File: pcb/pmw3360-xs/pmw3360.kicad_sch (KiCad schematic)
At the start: 16 parts, among them IC1001 AP7335-WG-7, J1001 Conn_01x01_Socket, J1002 Conn_01x01_Socket, J1004 Conn_01x01_Socket, J1005 Conn_01x01_Socket, J1006 Conn_01x01_Socket, J1007 Conn_01x01_Socket, U1001 PMW3360DM-T2QU

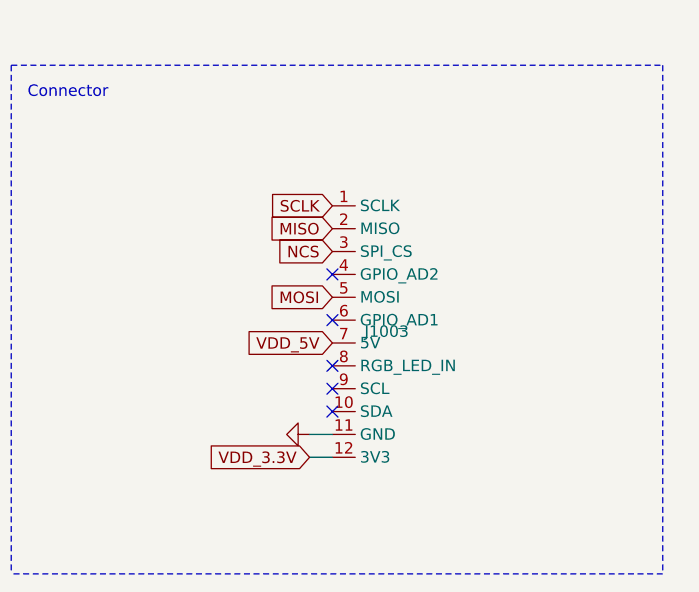
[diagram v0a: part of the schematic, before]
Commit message: updated vikm connector symbols, per some recommendations from sigprof in fingerpunch discord
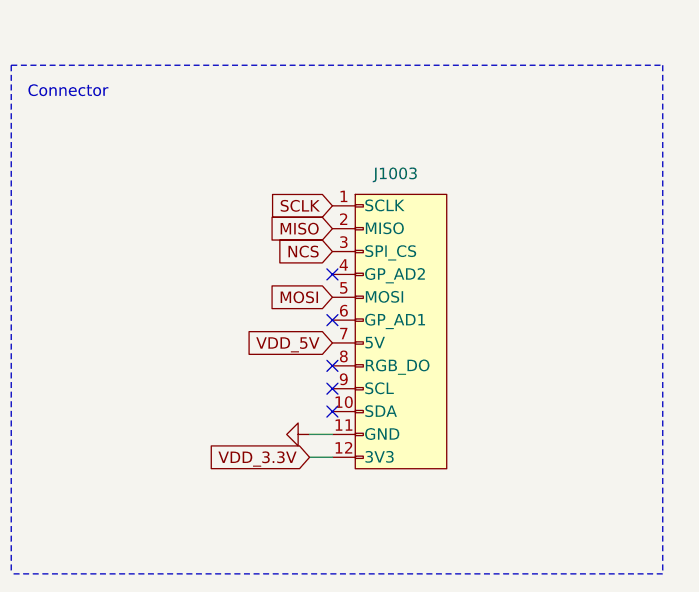
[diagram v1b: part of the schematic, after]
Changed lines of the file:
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@@
     )
   )
-  (symbol (lib_id "vik:vik-module-connector") (at 186.182 132.334 0) (unit 1)
-    (in_bom yes) (on_board yes) (dnp no) (fields_autoplaced)
-    (property "Reference" "J1003" (at 189.738 132.334 0)
+  (symbol (lib_id "vik:vik-module-connector") (at 193.802 131.064 0) (unit 1)
+    (in_bom yes) (on_board yes) (dnp no)
+    (property "Reference" "J1003" (at 190.754 114.808 0)
       (effects (font (size 1.27 1.27)) (justify left))
     )
-    (property "Value" "~" (at 186.182 125.984 0)
+    (property "Value" "~" (at 193.802 124.714 0)
       (effects (font (size 1.27 1.27)))
     )
-    (property "Footprint" "vik:vik-module-connector-horizontal" (at 186.182 125.984 0)
+    (property "Footprint" "vik:vik-module-connector-horizontal" (at 193.802 124.714 0)
       (effects (font (size 1.27 1.27)) hide)
     )
-    (property "Datasheet" "" (at 186.182 125.984 0)
+    (property "Datasheet" "" (at 193.802 124.714 0)
       (effects (font (size 1.27 1.27)) hide)
     )
-    (property "LCSC" "C2919557" (at 186.182 132.334 0)
+    (property "LCSC" "C2919557" (at 193.802 131.064 0)
       (effects (font (size 1.27 1.27)) hide)
     )

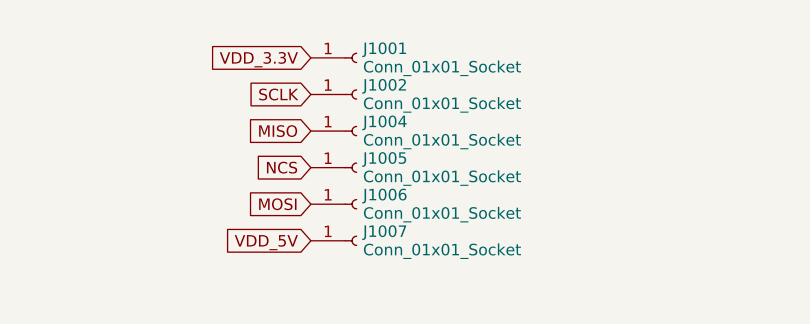
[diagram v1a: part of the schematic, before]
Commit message: added ground through hole for vik pmw3360 xs
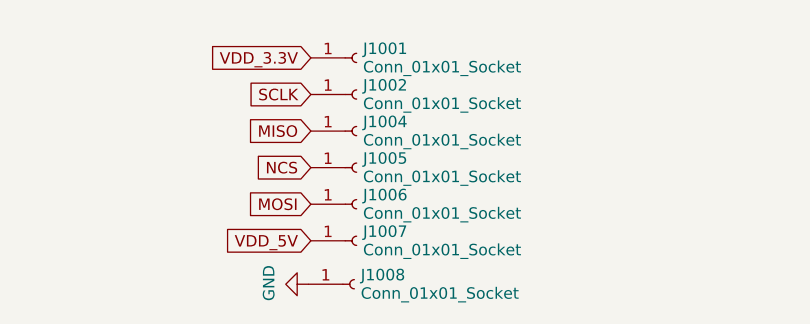
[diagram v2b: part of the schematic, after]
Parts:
- added J1008: Conn_01x01_Socket, Connector_Wire:SolderWire-0.5sqmm_1x01_D0.9mm_OD2.3mm, symbol Connector:Conn_01x01_Socket
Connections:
- net GND: now also J1008.1 (Pin_1)
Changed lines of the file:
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@@
+    )
+  )
+  (symbol (lib_id "Connector:Conn_01x01_Socket") (at 92.202 160.782 0) (unit 1)
+    (in_bom yes) (on_board yes) (dnp no) (fields_autoplaced)
+    (property "Reference" "J1008" (at 92.9132 159.758 0)
+      (effects (font (size 1.27 1.27)) (justify left))
+    )
+    (property "Value" "Conn_01x01_Socket" (at 92.9132 161.806 0)
+      (effects (font (size 1.27 1.27)) (justify left))
+    )
+    (property "Footprint" "Connector_Wire:SolderWire-0.5sqmm_1x01_D0.9mm_OD2.3mm" (at 92.202 160.782 0)
+      (effects (font (size 1.27 1.27)) hide)
+    )
+    (property "Datasheet" "~" (at 92.202 160.782 0)
+      (effects (font (size 1.27 1.27)) hide)
+    )
+    (pin "1")
+    (instances
+      (project "pmw3360"
+        (path "/e63e39d7-6ac0-4ffd-8aa3-1841a4541b55"
+          (reference "J1008") (unit 1)
+        )
+      )
     )
   )
@@
         )
       )
+    )
+  )
+  (symbol (lib_id "power:GND") (at 87.122 160.782 270) (mirror x) (unit 1)
+    (in_bom yes) (on_board yes) (dnp no)
+    (property "Reference" "#PWR01002" (at 80.772 160.782 0)
+      (effects (font (size 1.27 1.27)) hide)
+    )
+    (property "Value" "GND" (at 82.7278 160.655 0)
+      (effects (font (size 1.27 1.27)))
+    )
+    (property "Footprint" "" (at 87.122 160.782 0)
+      (effects (font (size 1.27 1.27)) hide)
+    )
+    (property "Datasheet" "" (at 87.122 160.782 0)
+      (effects (font (size 1.27 1.27)) hide)
+    )
+    (pin "1")
+    (instances
+      (project "pmw3360"
+        (path "/e63e39d7-6ac0-4ffd-8aa3-1841a4541b55"
+          (reference "#PWR01002") (unit 1)
+        )
+      )

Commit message: incorrect copyright messages in some of the schema files
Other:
- company: bastard keyboards -> (none)
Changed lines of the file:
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@@
   (paper "A4")
   (title_block
-    (company "bastard keyboards")
-    (comment 4 "Copyright Quentin Lebastard")
+    (comment 4 "https://github.com/sadekbaroudi/vik")
   )
   (junction (at 168.783 69.342) (diameter 1.016) (color 0 0 0 0)
